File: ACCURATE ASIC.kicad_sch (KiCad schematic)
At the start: 91 parts, among them IC12 ACCURATE_2A_JLCC28, IC13 DAC7578SRGE, IC14 CERN_aCCURATE2_A_Chip1, IC15 LM8272MMX, IC16 SHT4x, IC17 LM8272MMX, IC19 LTC2471IMS

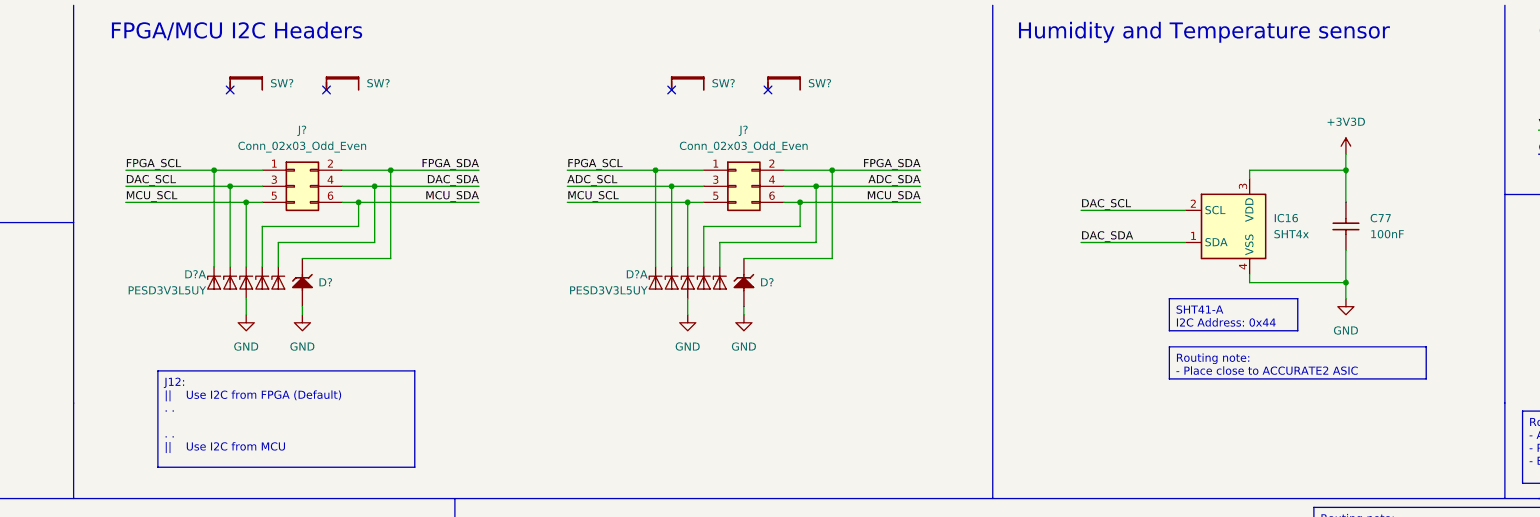
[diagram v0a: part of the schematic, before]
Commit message: Replaced the rest of the KiCADlib components with CERNlib ones
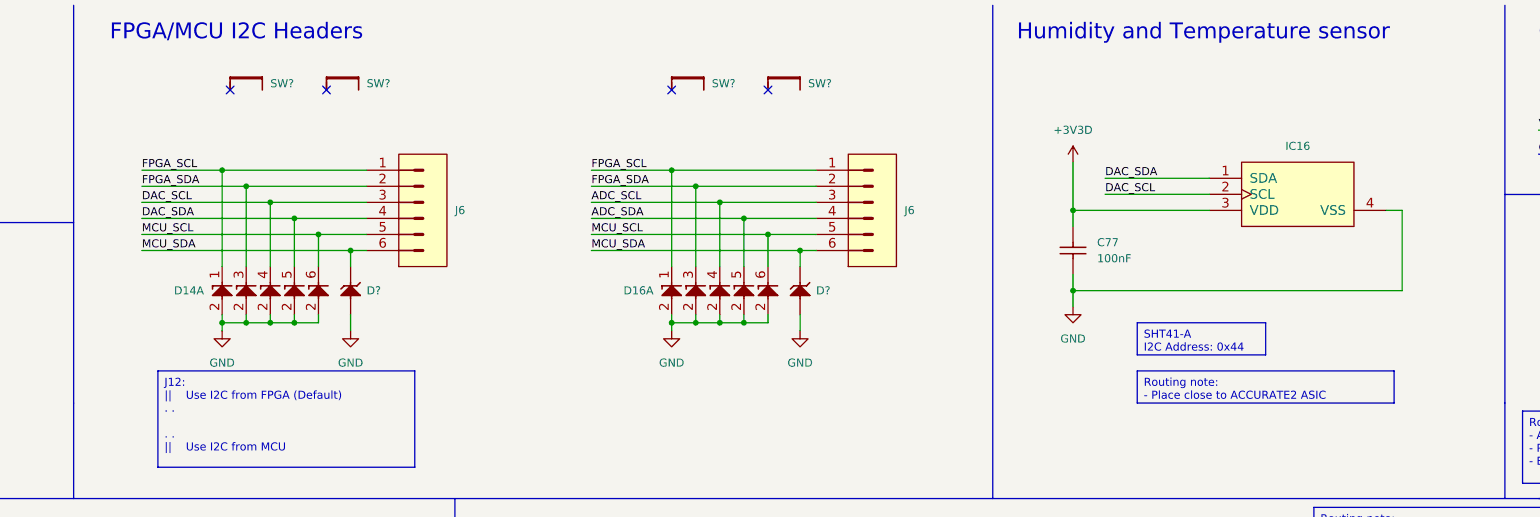
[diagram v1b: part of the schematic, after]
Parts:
- removed D? (x10): PESD3V3L5UY, Package_TO_SOT_SMD:SOT-363_SC-70-6, symbol Power_Protection:PESD3V3L5UY
- removed IC16: SHT4x, Sensor_Humidity:Sensirion_DFN-4_1.5x1.5mm_P0.8mm_SHT4x_NoCentralPad, symbol Sensor_Humidity:SHT4x
- removed J? (x2): Conn_02x03_Odd_Even, Connector_PinHeader_2.54mm:PinHeader_2x03_P2.54mm_Vertical, symbol Connector_Generic:Conn_02x03_Odd_Even
- added D14, D16: PESD3V3L5UY, ICs And Semiconductors SMD:SOT65P210X110-6N, symbol Diodes:PESD3V3L5UY
- added IC16: SHT41-AD1B, ICs And Semiconductors SMD:SON80P150X150X80-4N, symbol Sensors:SHT41-AD1B
- added J6 (x2): SAMTEC_TSW-103-23-L-D, SAMTEC THD:SAMTEC_TSW-103-23-L-D, symbol SAMTEC:SAMTEC_TSW-103-23-L-D
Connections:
- net +3V3D: now also IC16.3 (VDD)
- net ADC_SCL: now also D16.4 (C), J6.3
- net ADC_SDA: now also D16.5 (C), J6.4
- net DAC_SCL: now also D14.4 (C), IC16.2 (SCL), J6.3
- net DAC_SDA: now also D14.5 (C), IC16.1 (SDA), J6.4
- net FPGA_SCL: now also D14.1 (C), D16.1 (C), J6.1, J6.1
- net FPGA_SDA: now also D14.3 (C), D16.3 (C), J6.2, J6.2; no longer D?.1 (C), D?.1 (C)
- net GND: now also D14.2 (A), D14.2 (A), D14.2 (A), D14.2 (A), D14.2 (A), D16.2 (A), D16.2 (A), D16.2 (A), D16.2 (A), D16.2 (A), IC16.4 (VSS)
- net MCU_SCL: now also D14.6 (C), D16.6 (C), J6.5, J6.5
- net MCU_SDA: now also D?.1 (C), D?.1 (C), J6.6, J6.6
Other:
- moved on the sheet: C77, D?

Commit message: Updated schematic after routing, added wiki link to the readme
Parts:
- IC12: footprint ICs And Semiconductors SMD:CERN_ACCURATE_2A_JLCC28 -> ICs And Semiconductors SMD:CERN_aCCURATE_JLCC28
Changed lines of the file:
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@@
       (effects (font (size 1.27 1.27)) (justify left) hide)
     )
-    (property "Footprint" "ICs And Semiconductors SMD:CERN_ACCURATE_2A_JLCC28" (at 236.22 184.15 0)
+    (property "Footprint" "ICs And Semiconductors SMD:CERN_aCCURATE_JLCC28" (at 236.22 184.15 0)
       (effects (font (size 1.27 1.27)) (justify left) hide)
     )

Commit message: Updated schematic after routing, added layout
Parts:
- removed C55, C57, C62, C70, C74, C75, C76, C77, C79, C80, C82, C84, C85, C87, C88: CC0603_100NF_50V_10%_X7R, Capacitors SMD:CAPC1608X87N, symbol Capacitors SMD:CC0603_100NF_50V_10%_X7R
- removed C56, C58, C61, C69, C71, C72, C78, C81, C83, C86: CC0603_10UF_25V_20%_X5R, Capacitors SMD:CAPC1709X100N, symbol Capacitors SMD:CC0603_10UF_25V_20%_X5R
- removed C59, C60, C63, C64, C65, C66, C67, C68: CC0603_470PF_50V_5%_NP0, Capacitors SMD:CAPC1608X87N, symbol Capacitors SMD:CC0603_470PF_50V_5%_NP0
- removed C73: CC1206_100NF_50V_10%_X7R, Capacitors SMD:CAPC3216X140N, symbol Capacitors SMD:CC1206_100NF_50V_10%_X7R
- removed D14, D16: PESD3V3L5UY, ICs And Semiconductors SMD:SOT65P210X110-6N, symbol Diodes:PESD3V3L5UY
- removed D? (x2): SMBJ3V3, ICs And Semiconductors SMD:DIOM5436X244N, symbol Diodes:SMBJ3V3
- removed IC12: ACCURATE_2A_JLCC28, ICs And Semiconductors SMD:CERN_aCCURATE_JLCC28, symbol Analog & Interface:ACCURATE_2A_JLCC28
- removed IC13: DAC7578SRGE, ICs And Semiconductors SMD:QFN50P400X400X100-25N-S280, symbol Analog & Interface:DAC7578SRGE
- removed IC14: CERN_aCCURATE2_A_Chip1, ICs And Semiconductors Bonding:CERN_aCCURATE1, symbol Bonding:CERN_aCCURATE2_A_Chip1
- removed IC15, IC17: LM8272MMX, ICs And Semiconductors SMD:SOP65P490X110-8N, symbol Operational Amplifiers:LM8272MMX
- removed IC16: SHT41-AD1B, ICs And Semiconductors SMD:SON80P150X150X80-4N, symbol Sensors:SHT41-AD1B
- removed IC19: LTC2471IMS, ICs And Semiconductors SMD:SOP65P490X110-12N, symbol Analog & Interface:LTC2471IMS
- removed J6 (x2): SAMTEC_TSW-103-23-L-D, SAMTEC THD:SAMTEC_TSW-103-23-L-D, symbol SAMTEC:SAMTEC_TSW-103-23-L-D
- removed MSBOX1: MSBOX_PERANCEA_PFL6T, Metal Screening Box:MSBOX_PERANCEA_PFL6T, symbol Metal Screening Box:MSBOX_PERANCEA_PFL6T
- removed PB?: PB_C&K_KSC321JLFS, Switches:PB_C&K_KSC321J, symbol Switches:PB_C&K_KSC321JLFS
- removed R37: R0603_10K_1%_0.1W_100PPM, Resistors SMD:RESC1608X55N, symbol Resistors SMD:R0603_10K_1%_0.1W_100PPM
- removed R46, R47, R48, R49, R50, R51, R52, R53, R54: R0603_0R_JUMPER, Resistors SMD:RESC1608X55N, symbol Resistors SMD:R0603_0R_JUMPER
- removed SW? (x4): HARWIN_M50-1900005, symbol HARWIN:HARWIN_M50-1900005
- removed TP18, TP19, TP20, TP21, TP22, TP23, TP24, TP25, TP26, TP27, TP28, TP29, TP30, TP31, TP32, TP33, TP34, TP35, TP36, TP37: SMD_PAD_1.27X1.27MM, Pads:TPS127, symbol Pads:SMD_PAD_1.27X1.27MM
- added C10, C11, C12, C13, C6, C7, C8, C9: CC0603_470PF_50V_5%_NP0, Capacitors SMD:CAPC1608X87N, symbol Capacitors SMD:CC0603_470PF_50V_5%_NP0
- added C14, C15, C20, C24, C27, C29, C3, C4: CC0603_10UF_25V_20%_X5R, Capacitors SMD:CAPC1709X100N, symbol Capacitors SMD:CC0603_10UF_25V_20%_X5R
- added C16: CC1206_100NF_50V_10%_X7R, Capacitors SMD:CAPC3216X140N, symbol Capacitors SMD:CC1206_100NF_50V_10%_X7R
- added C17, C18, C19, C2, C21, C22, C23, C25, C26, C28, C30, C31, C5: CC0603_100NF_50V_10%_X7R, Capacitors SMD:CAPC1608X87N, symbol Capacitors SMD:CC0603_100NF_50V_10%_X7R
- added D3, D5: PESD3V3L5UY, ICs And Semiconductors SMD:SOT65P210X110-6N, symbol Diodes:PESD3V3L5UY
- added D4, D6: PESD3V3S1UB, ICs And Semiconductors SMD:SODFL1608X65N, symbol Diodes:PESD3V3S1UB
- added IC1: DAC7578SRGE, ICs And Semiconductors SMD:QFN50P400X400X100-25N-S280, symbol Analog & Interface:DAC7578SRGE
- added IC2, IC3: LM8272MMX, ICs And Semiconductors SMD:SOP65P490X110-8N, symbol Operational Amplifiers:LM8272MMX
- added IC4: ACCURATE_2A_JLCC28, ICs And Semiconductors SMD:CERN_aCCURATE_JLCC28, symbol Analog & Interface:ACCURATE_2A_JLCC28
- added IC5: SHT41-AD1B, ICs And Semiconductors SMD:SON80P150X150X80-4N, symbol Sensors:SHT41-AD1B
- added IC6: CERN_aCCURATE2_A_Chip1, ICs And Semiconductors BONDING:CERN_aCCURATE1, symbol Bonding:CERN_aCCURATE2_A_Chip1
- added IC7: LTC2471IMS, ICs And Semiconductors SMD:SOP65P490X110-12N, symbol Analog & Interface:LTC2471IMS
- added J6, J7: SAMTEC_HTSW-103-23-L-D, SAMTEC THD:SAMTEC_HTSW-103-23-L-D, symbol SAMTEC:SAMTEC_HTSW-103-23-L-D
- added MSBOX1: MSBOX_PERANCEA_PFL6T, Metal Screening Box:MSBOX_PERANCEA_PFL2T, symbol Metal Screening Box:MSBOX_PERANCEA_PFL2T
- added PB2: PB_C&K_KSC321JLFS, Switches:PB_C&K_KSC321J, symbol Switches:PB_C&K_KSC321JLFS
- added R10, R11, R12, R13, R15, R6, R7, R8, R9: R0603_0R_JUMPER, Resistors SMD:RESC1608X55N, symbol Resistors SMD:R0603_0R_JUMPER
- added R14: R0603_10K_1%_0.1W_100PPM, Resistors SMD:RESC1608X55N, symbol Resistors SMD:R0603_10K_1%_0.1W_100PPM
- added SW1, SW2, SW3, SW4: HARWIN_M50-1900005, COMATEL THD:STELVIO-KONTEK_3131730000400, symbol STELVIO-KONTEK COMATEL:STELVIO-KONTEK_3131730000400
- added TP10, TP11, TP12, TP13, TP14, TP15, TP16, TP17, TP18, TP19, TP20, TP21, TP22, TP23, TP24, TP5, TP6, TP7, TP8, TP9: HARWIN_S1751-46, HARWIN SMD:HARWIN_S1751-46, symbol HARWIN:HARWIN_S1751-46
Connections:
- net +3V3A: now also C2.1, C20.1, C21.1, C28.1, C29.1, C3.1, C4.1, C5.1, IC1.12 (~{CLR}), IC1.2 (AVDD), IC1.9 (RSTSEL), IC2.8 (V+), IC2.8 (V+), IC3.8 (V+), IC3.8 (V+), IC7.12 (VCC)
- net +3V3D: now also C22.1, IC5.3 (VDD)
- net 3V3_REF: now also C23.1, C24.1, IC4.25 (VDD), IC6.23, R14.2
- net 3V_REF: now also IC1.8 (VREFIN)
- net A1_Vbias1: now also C6.1, IC4.1 (VBIAS1), IC6.1, R13.2, TP6.1
- net A1_Vbias3: now also C13.1, IC4.10 (VBIAS3), IC6.9, R6.2, TP13.1
- net A1_Vcharge+: now also C9.1, IC2.3 (IN+), R8.2, TP9.1
- net A1_Vcharge+_buf: now also C15.1, C18.1, IC2.1 (OUT), IC2.2 (IN-), IC4.6 (VCHARGE+), IC6.6, TP5.1
- net A1_Vth1: now also C8.1, IC4.27 (VTH1), IC4.5 (VBIAS2), IC6.25, IC6.5, R12.2, TP8.1
- net A1_Vth2: now also C10.1, IC4.26 (VTH2), IC6.24, R11.2, TP10.1
- net A1_Vth3: now also C12.1, IC4.24 (VTH3), IC6.22, R10.2, TP12.1
- net A1_Vth4: now also C11.1, IC4.8 (VTH4), IC6.7, R7.2, TP11.1
- net ACCURATE_RESET: now also IC4.22 (RESET1), IC6.20, PB2.1, PB2.2, R14.1
- net ADC_SCL: now also D5.4 (C), IC7.5 (SCL), J7.3
- net ADC_SDA: now also D5.5 (C), IC7.6 (SDA), J7.4
- net Comp1: now also IC4.19 (COMP1), IC6.18, TP20.1
- net Comp2: now also IC4.18 (COMP2), IC6.17, TP21.1
- net Comp3: now also IC4.17 (COMP3), IC6.16, TP22.1
- net Comp4: now also IC4.16 (COMP4), IC6.15, TP23.1
- net Current_In: now also C16.2, IC4.2 (IN1), IC6.2
- net DAC_SCL: now also D3.4 (C), IC1.20 (SCL), IC5.2 (SCL), J6.3
- net DAC_SDA: now also D3.5 (C), IC1.19 (SDA), IC5.1 (SDA), J6.4
- net Enable.High: now also IC4.15 (ENABLE_HIGH), IC6.14, TP15.1
- net Enable.Low: now also IC4.13 (ENABLE_LOW), IC6.12, TP17.1
- net Enable.Medium: now also IC4.14 (ENABLE_MED), IC6.13, TP16.1
- net FPGA_CLK: now also IC4.20 (CAP_CLK), IC6.19, TP19.1
- net FPGA_SCL: now also D3.1 (C), D5.1 (C), J6.1, J7.1, SW1.1, SW3.1
- net FPGA_SDA: now also D3.3 (C), D5.3 (C), J6.2, J7.2, SW2.1, SW4.1
- net GND: now also C10.2, C11.2, C12.2, C13.2, C14.2, C15.2, C17.2, C18.2, C19.2, C2.2, C20.2, C21.2, C22.2, C23.2, C24.2, C25.2, C26.2, C27.2, C28.2, C29.2, C3.2, C30.2, C31.2, C4.2, C5.2, C6.2, C7.2, C8.2, C9.2, D3.2 (A), D3.2 (A), D3.2 (A), D3.2 (A), D3.2 (A), D4.2 (A), D5.2 (A), D5.2 (A), D5.2 (A), D5.2 (A), D5.2 (A), D6.2 (A), IC1.10 (ADDR1), IC1.11 (ADDR0), IC1.17 (GND), IC1.21 (TWOC), IC1.22 (~{LDAC}), IC1.25 (EP), IC2.4 (V-), IC2.4 (V-), IC3.4 (V-), IC3.4 (V-), IC4.11 (VSS), IC5.4 (VSS), IC6.10, IC7.10 (GND), IC7.11 (GND), IC7.3 (AO), IC7.4 (GND), IC7.7 (GND), IC7.8 (REF-), MSBOX1.1, MSBOX1.10, MSBOX1.2, MSBOX1.3, MSBOX1.4, MSBOX1.5, MSBOX1.6, MSBOX1.7, MSBOX1.8, MSBOX1.9, PB2.3, PB2.4
- net MCU_SCL: now also D3.6 (C), D5.6 (C), J6.5, J7.5
- net MCU_SDA: now also D4.1 (C), D6.1 (C), J6.6, J7.6
- net OTA_Out: now also IC2.5 (IN+), R15.2
- net OTA_Out_Buf: now also IC2.6 (IN-), IC2.7 (OUT), IC7.9 (IN), TP24.1
- net Vcm: now also C7.1, IC3.3 (IN+), IC3.5 (IN+), R9.2, TP7.1
- net Vcm_Buf: now also C14.1, C16.1, C17.1, C26.1, C27.1, IC3.1 (OUT), IC3.2 (IN-), IC4.3 (VCM), IC6.3, TP18.1
- net Vcmd: now also C19.1, C25.1, IC3.6 (IN-), IC3.7 (OUT), IC4.28 (VCHARGE-), IC4.9 (VCMD), IC6.26, IC6.8, TP14.1
- new net: C30.1, IC7.2 (COMP)
- new net: IC1.4 (VOUTC), R12.1
- new net: IC1.15 (VOUTD), R8.1
- new net: IC1.5 (VOUTE), R11.1
- new net: IC1.13 (VOUTH), R6.1
- new net: IC1.3 (VOUTA), R13.1
- new net: C31.1, IC7.1 (REFOUT)
- new net: IC1.16 (VOUTB), R9.1
- new net: IC6.D1 (Vbias1), IC6.L1
- new net: IC6.D10 (Vss), IC6.L10
- new net: IC6.D12 (En_Low), IC6.L12
- new net: IC6.D13 (En_Med), IC6.L13
- new net: IC6.D14 (En_High), IC6.L14
- new net: IC6.D15 (Comp4), IC6.L15
- new net: IC6.D16 (Comp3), IC6.L16
- new net: IC6.D17 (Comp2), IC6.L17
- new net: IC6.D18 (Comp1), IC6.L18
- new net: IC6.D19 (Cap_clk), IC6.L19
- new net: IC6.D2 (In1), IC6.L2
- new net: IC6.D20 (Reset1), IC6.L20
- new net: IC6.D21 (OTA1_Out), IC6.L21
- new net: IC6.D22 (Vth3), IC6.L22
- new net: IC6.D23 (Vdd), IC6.L23
- new net: IC6.D24 (Vth2), IC6.L24
- new net: IC6.D25 (Vth1), IC6.L25
- new net: IC6.D26 (Vcharge-), IC6.L26
- new net: IC6.D3 (Vcm), IC6.L3
- new net: IC6.D5 (Vbias2), IC6.L5
- new net: IC6.D6 (Vcharge+), IC6.L6
- new net: IC6.D7 (Vth4), IC6.L7
- new net: IC6.D8 (Vcmd), IC6.L8
- new net: IC6.D9 (Vbias3), IC6.L9
- new net: IC1.14 (VOUTF), R7.1
- new net: IC1.6 (VOUTG), R10.1
- new net NC_NetIC12-12: IC4.12 (NC), IC6.11
- new net NC_NetIC12-4: IC4.4 (NC), IC6.4
- new net OTA1_Out: IC4.23 (OTA1_OUT), IC6.21, R15.1
- no-connect marks 91 -> 31

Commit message: Annotation now matches the produced PCB
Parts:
- renumbered C2 to C55, C4 to C56, C5 to C57, C3 to C58, C6 to C59, C7 to C60, C8 to C63, C9 to C64, C10 to C65, C11 to C66, C12 to C67, C13 to C68, C20 to C69, C21 to C70, C14 to C71, C15 to C72, C16 to C73, C17 to C74, C18 to C75, C19 to C76, C22 to C77, C28 to C80, C29 to C81, C23 to C82, C24 to C83, C25 to C84, C26 to C85, C27 to C86, C30 to C87, C31 to C88, D3 to D14, D4 to D15, D5 to D16, D6 to D17, IC4 to IC12, IC1 to IC13, IC6 to IC14, IC2 to IC15, IC5 to IC16, IC3 to IC17, IC7 to IC19, J6 to J17, J7 to J18, PB2 to PB5, R6 to R46, R7 to R47, R8 to R48, R9 to R49, R10 to R50, R11 to R51, R12 to R52, R13 to R53, R15 to R54, R14 to R61, SW3 to SW10, SW4 to SW11, SW1 to SW8, SW2 to SW9, TP5 to TP18, TP6 to TP19, TP7 to TP20, TP8 to TP21, TP9 to TP22, TP10 to TP23, TP11 to TP24, TP14 to TP25, TP12 to TP26, TP13 to TP27, TP19 to TP28, TP18 to TP29, TP20 to TP30, TP21 to TP31, TP22 to TP32, TP23 to TP33, TP15 to TP34, TP16 to TP35, TP17 to TP36, TP24 to TP37

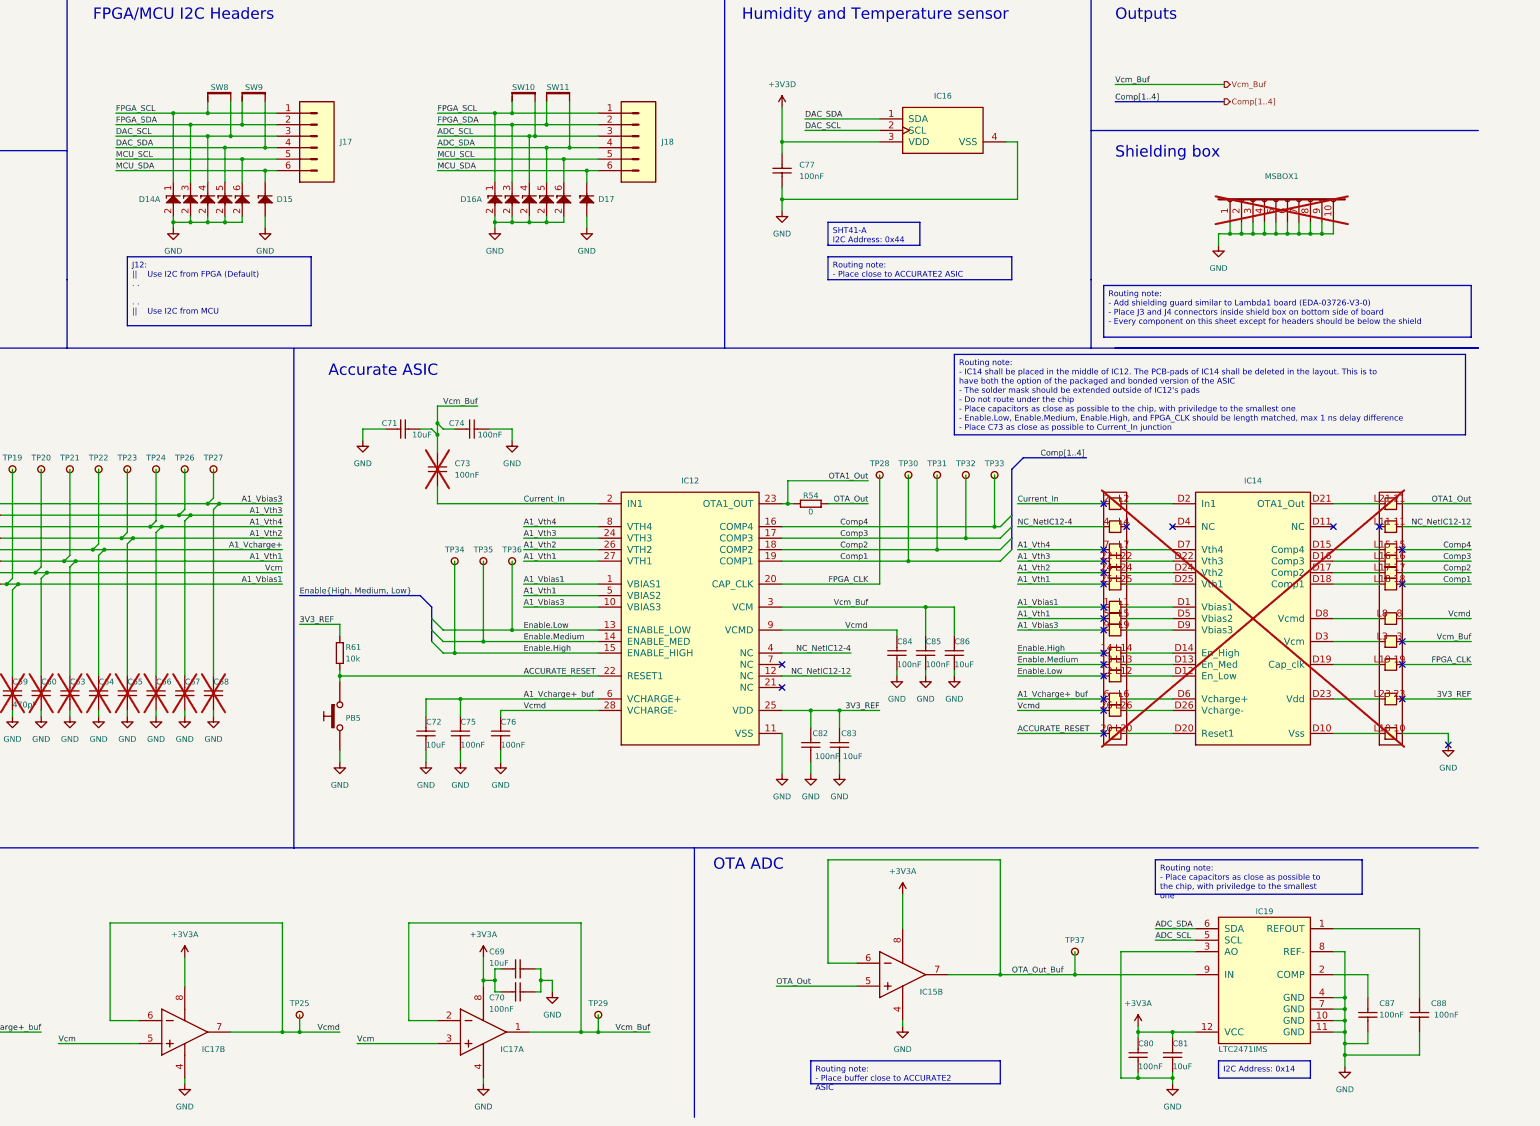
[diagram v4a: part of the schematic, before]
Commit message: Fixed reset circuits, removed 1V2 LED, fixing 2V5 circuit, added pullups to FPGA I2C, moved PSU TPs and JMPrs, replaced OSC2, removed ADC, added 2232 DTR, removed PSU seq TPs, replaced 2V5 LED res
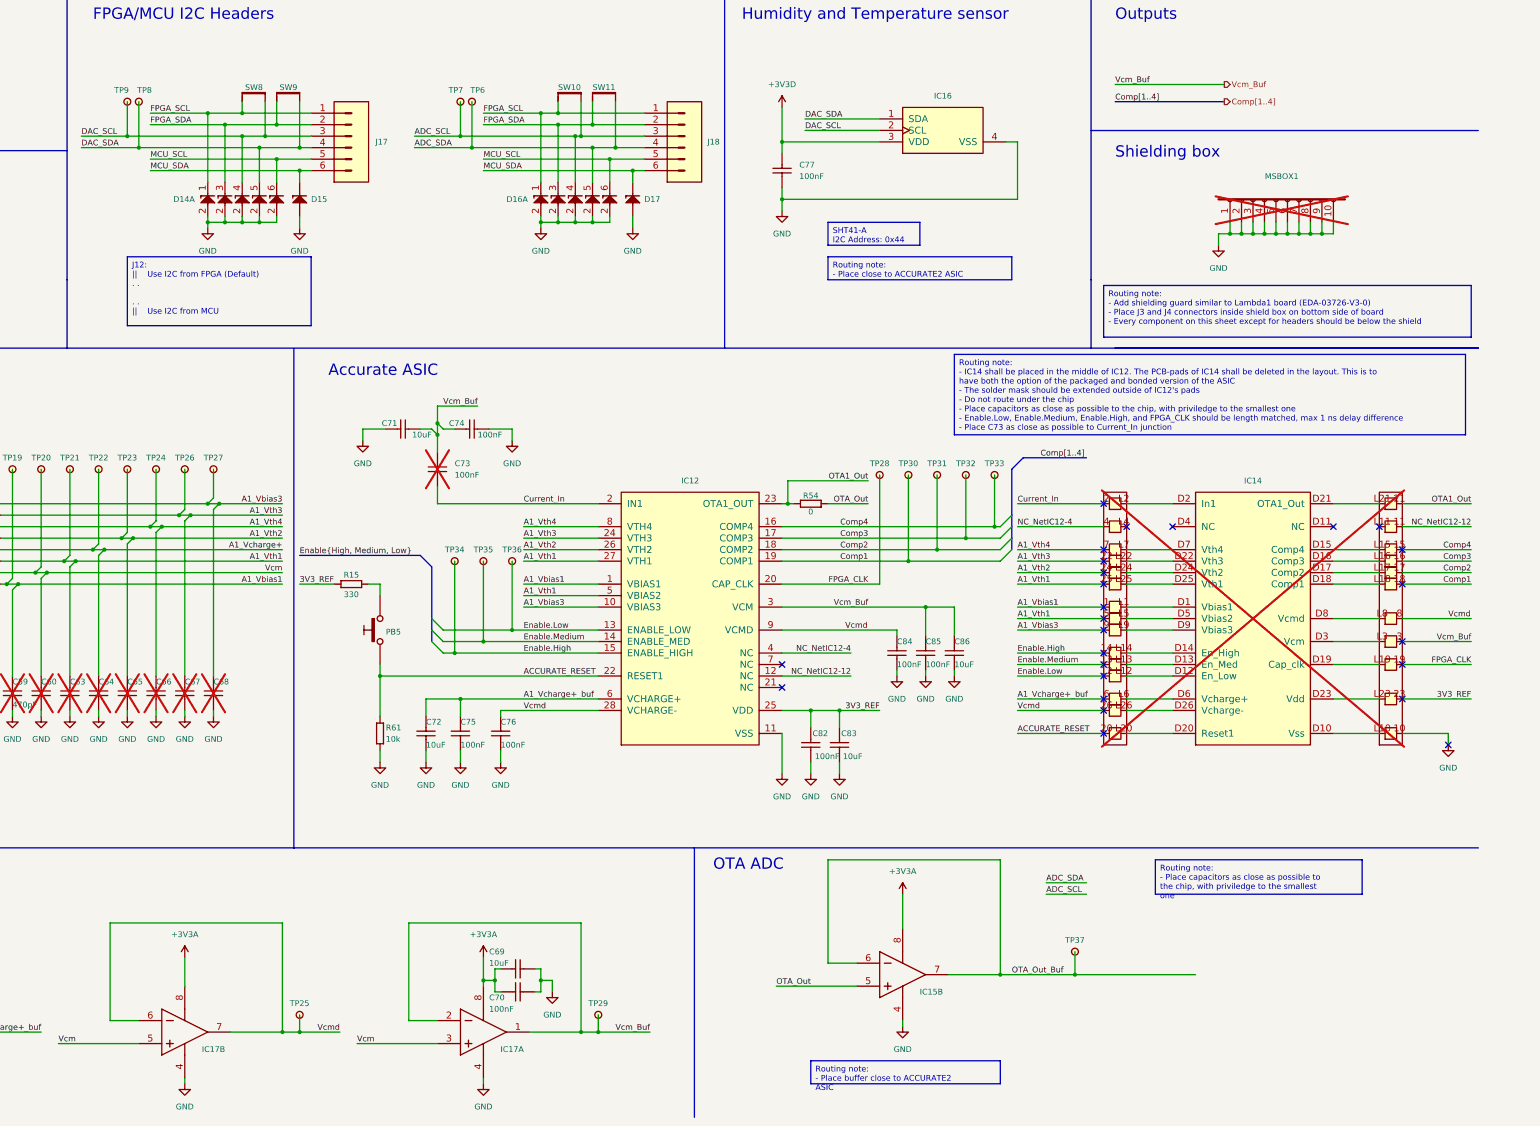
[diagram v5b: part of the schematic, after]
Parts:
- removed C80, C87, C88: CC0603_100NF_50V_10%_X7R, Capacitors SMD:CAPC1608X87N, symbol Capacitors SMD:CC0603_100NF_50V_10%_X7R
- removed C81: CC0603_10UF_25V_20%_X5R, Capacitors SMD:CAPC1709X100N, symbol Capacitors SMD:CC0603_10UF_25V_20%_X5R
- removed IC19: LTC2471IMS, ICs And Semiconductors SMD:SOP65P490X110-12N, symbol Analog & Interface:LTC2471IMS
- added R15: R0603_330R_1%_0.1W_100PPM, Resistors SMD:RESC1608X55N, symbol Resistors SMD:R0603_330R_1%_0.1W_100PPM
- added TP6, TP7, TP8, TP9: HARWIN_S1751-46, HARWIN SMD:HARWIN_S1751-46, symbol HARWIN:HARWIN_S1751-46
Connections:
- net 3V3_REF: now also R15.1; no longer R61.2
- net ACCURATE_RESET: now also PB5.3, PB5.4, R61.2; no longer PB5.1, PB5.2, R61.1
- net ADC_SCL: now also TP7.1
- net ADC_SDA: now also TP6.1
- net DAC_SCL: now also TP9.1
- net DAC_SDA: now also TP8.1
- net GND: now also R61.1; no longer PB5.3, PB5.4
- new net: PB5.1, PB5.2, R15.2
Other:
- moved on the sheet: D14A, D15, D16A, D17, J17, J18, SW10, SW11, SW8, SW9

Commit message: Added new ADC
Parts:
- removed C59, C60, C63, C64, C65, C66, C67, C68: CC0603_470PF_50V_5%_NP0, Capacitors SMD:CAPC1608X87N, symbol Capacitors SMD:CC0603_470PF_50V_5%_NP0
- removed PB5: PB_C&K_KSC321JLFS, Switches:PB_C&K_KSC321J, symbol Switches:PB_C&K_KSC321JLFS
- removed R15: R0603_330R_1%_0.1W_100PPM, Resistors SMD:RESC1608X55N, symbol Resistors SMD:R0603_330R_1%_0.1W_100PPM
- removed R61: R0603_10K_1%_0.1W_100PPM, Resistors SMD:RESC1608X55N, symbol Resistors SMD:R0603_10K_1%_0.1W_100PPM
- added C59, C60: CC0603_22NF_50V_10%_X7R, Capacitors SMD:CAPC1608X87N, symbol Capacitors SMD:CC0603_22NF_50V_10%_X7R
- added C63: CC0603_220NF_10V_10%_X7R, Capacitors SMD:CAPC1608X87N, symbol Capacitors SMD:CC0603_220NF_10V_10%_X7R
- added C78: CC0603_100NF_50V_10%_X7R, Capacitors SMD:CAPC1608X87N, symbol Capacitors SMD:CC0603_100NF_50V_10%_X7R
- added IC18: ADS1114IDGS, symbol Analog & Interface:ADS1114
- added R15, R61: R0603_0R_JUMPER, Resistors SMD:RESC1608X55N, symbol Resistors SMD:R0603_0R_JUMPER
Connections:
- net +3V3A: now also C78.1, IC18.1 (ADDR), IC18.8 (VDD)
- net ADC_SCL: now also IC18.10 (SCL)
- net ADC_SDA: now also IC18.9 (SDA)
- net GND: now also C59.2, C60.2, C78.2, IC18.3 (GND)
- net OTA_Out_Buf: now also R61.2
- net Vcm: now also R15.2
- new net: C60.1, C63.1, IC18.5 (AIN1), R15.1
- new net: C59.1, C63.2, IC18.4 (AIN0), R61.1
- no-connect marks 31 -> 34
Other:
- moved on the sheet: IC15B, TP37
